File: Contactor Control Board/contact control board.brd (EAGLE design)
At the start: 75.9 x 50.8 mm, 36 parts, among them Q1 2n2222, Q2 2n2222, Q3 2n2222, Q4 MOSFET-NCHANNELFQP30N06L

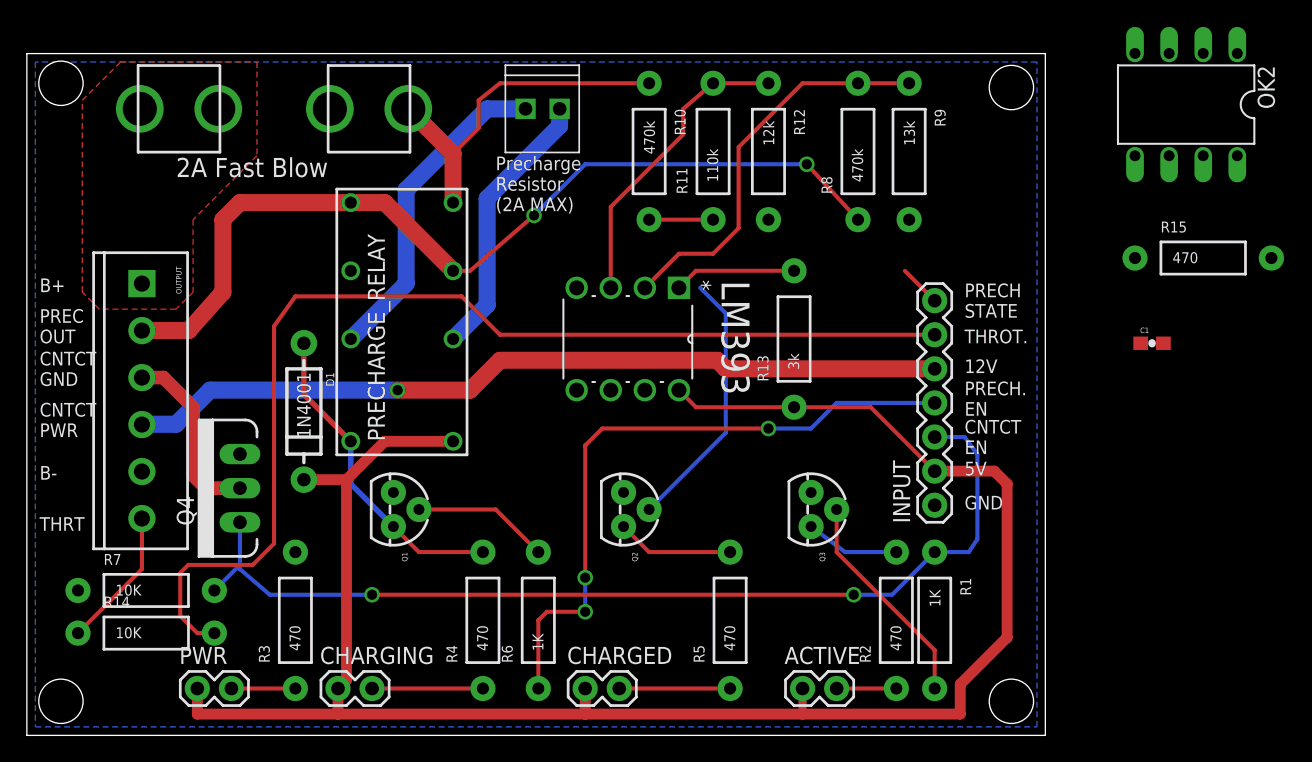
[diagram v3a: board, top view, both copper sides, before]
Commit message: Added buffer to use the output of the Op-Amp and split
it between an indicator LED and a digital signal output. Tested and
validated using breadboards
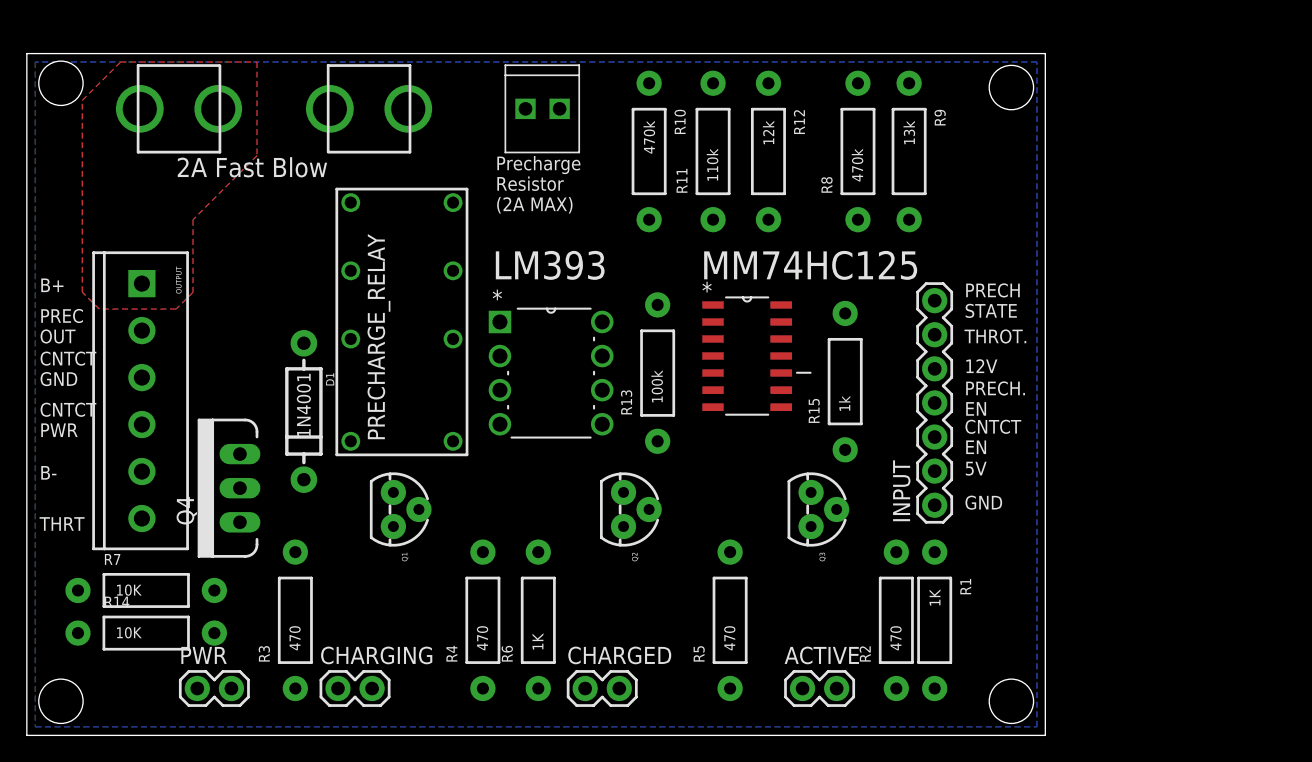
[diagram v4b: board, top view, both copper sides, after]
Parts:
- removed C1: 0.1uF, SparkFun-Capacitors:0603-CAP
- removed OK2: 6N138, optocoupler:DIL08
- added MM74HC125: MM74HC125M, Fairchild_By_element14_Batch_1:SOIC127P600X175-14N
- R13: value 3k -> 100k
- R15: value 470 -> 1k
- moved R15 28.2 mm to (61.0, 26.4), turned to 90 degrees
- moved R13 10.5 mm to (47.0, 27.0)
- moved LM393 3.17 mm to (42.9, 23.2), turned to 0 degrees
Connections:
- removed net PRECH_STATE: INPUT.7, OK2.6, Q2.2, R15.P$2
- removed net PRECH_STATE_TO_OPTO: LM393.1, OK2.2, R13.P$2
- new net N$6: MM74HC125.6, R15.P$2
- new net PRECH_STATE_LED: Q2.2, R15.P$1
- new net PRECH_STATE_OUT: INPUT.7, MM74HC125.3
- new net PRECH_STATE_TO_BUFF: LM393.1, MM74HC125.2, MM74HC125.5, R13.P$2
- net 5V: now also MM74HC125.14; no longer C1.1, OK2.8, R15.P$1
- net GND: now also MM74HC125.1, MM74HC125.4, MM74HC125.7; no longer C1.2, OK2.3, OK2.5
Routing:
- net 5V: track 138.5 -> 0.00 mm
- net THROTTLE: track 81.9 -> 0.00 mm
- net CONTACT_EN: track 73.8 -> 0.00 mm, vias 2 -> 0
- net PRECHARGE_OUT: track 67.6 -> 0.00 mm, vias 2 -> 0
- net 12V: track 61.3 -> 0.00 mm, vias 1 -> 0
- net PRECHARGE_EN: track 48.6 -> 0.00 mm, vias 3 -> 0
- net CAP_CHARGE_V_CURR: track 29.5 -> 0.00 mm
- net 72V_IN_FUSED: track 26.3 -> 0.00 mm
- net PRECHARGE_RESISTOR_OUT: track 24.2 -> 0.00 mm
- net PRECH_TRAN_COLLECTOR: track 23.9 -> 0.00 mm
- net PRECH_STATE: track 22.8 -> 0.00 mm
- net CAP_CHARGE_REF: track 22.6 -> 0.00 mm
- net PRECHARGE_RESISTOR_IN: track 20.4 -> 0.00 mm
- net N$2: track 16.4 -> 0.00 mm
- net CONTACT_GND: track 13.7 -> 0.00 mm
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
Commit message: Using the proper chip package for the buffer chip
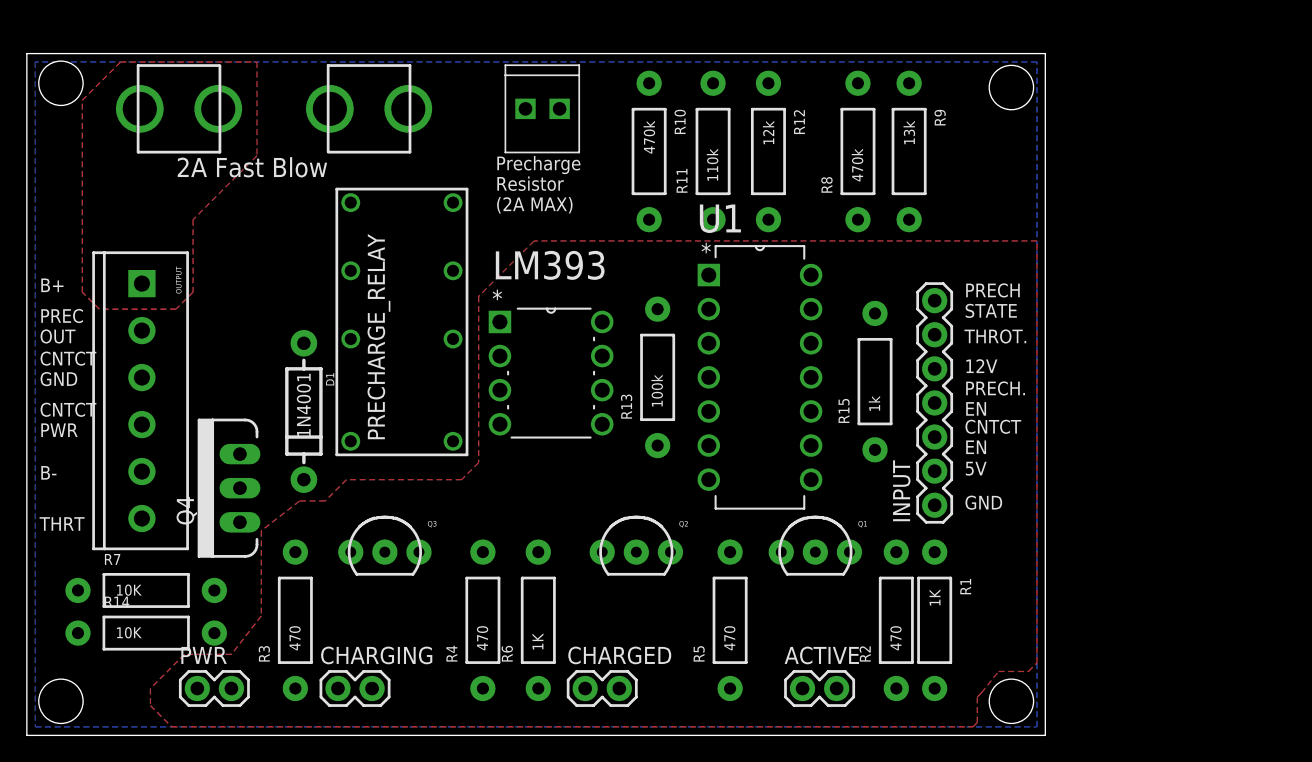
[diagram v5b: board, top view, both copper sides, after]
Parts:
- removed MM74HC125: MM74HC125M, Fairchild_By_element14_Batch_1:SOIC127P600X175-14N
- added U1: MM74HC125N, mm74hc125n:DIP254P762X533-14
- Q1, Q2, Q3: device SparkFun-DiscreteSemi:TO-92 -> SparkFun-DiscreteSemi:TO-92-AMMO
- moved Q3 31.9 mm to (26.7, 13.7), turned to 0 degrees
- moved Q1 31.6 mm to (58.7, 13.7), turned to 0 degrees
- moved Q2 3.31 mm to (45.4, 13.7), turned to 0 degrees
- moved R15 2.22 mm to (63.2, 26.4)
- moved R13 0.32 mm to (47.0, 26.7)
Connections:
- net 5V: now also U1.14; no longer MM74HC125.14
- net GND: now also U1.1, U1.4, U1.7; no longer MM74HC125.1, MM74HC125.4, MM74HC125.7
- net N$1: now also Q1.3; no longer Q3.3
- net N$2: now also Q1.2; no longer Q3.2
- net N$5: now also Q3.3; no longer Q2.3
- net N$6: now also U1.6; no longer MM74HC125.6
- net PRECH_STATE_LED: now also Q3.2; no longer Q2.2
- net PRECH_STATE_OUT: now also U1.3; no longer MM74HC125.3
- net PRECH_STATE_TO_BUFF: now also U1.2, U1.5; no longer MM74HC125.2, MM74HC125.5
- net PRECH_TRAN_COLLECTOR: now also Q2.3; no longer Q1.3
- net PRECH_TRAN_IN: now also Q2.2; no longer Q1.2
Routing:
- added copper zone on layer 1, net 5V

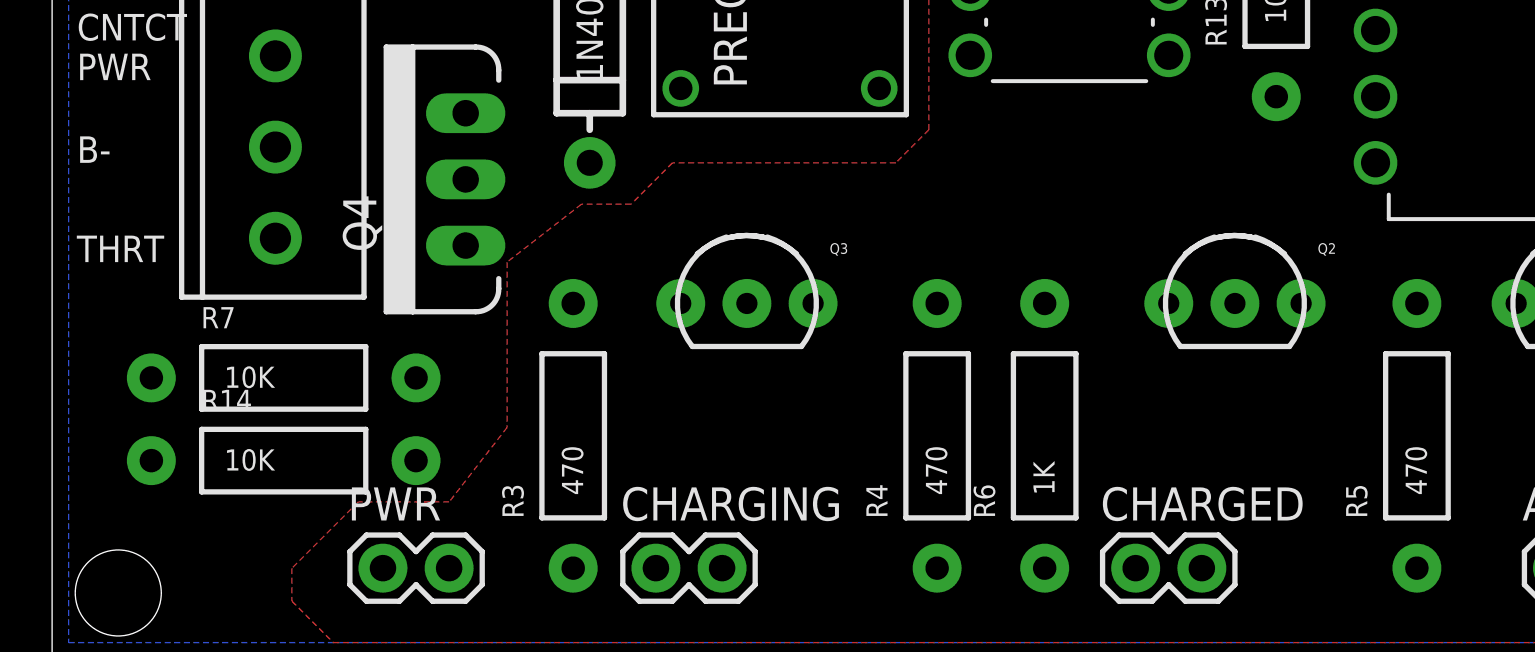
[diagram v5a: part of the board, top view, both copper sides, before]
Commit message: Updated precharge design
Replaced transistor with a FET as the Arduino can't source enough
current to trigger both the relay and the LED... At least not with the
transistors which were specced.
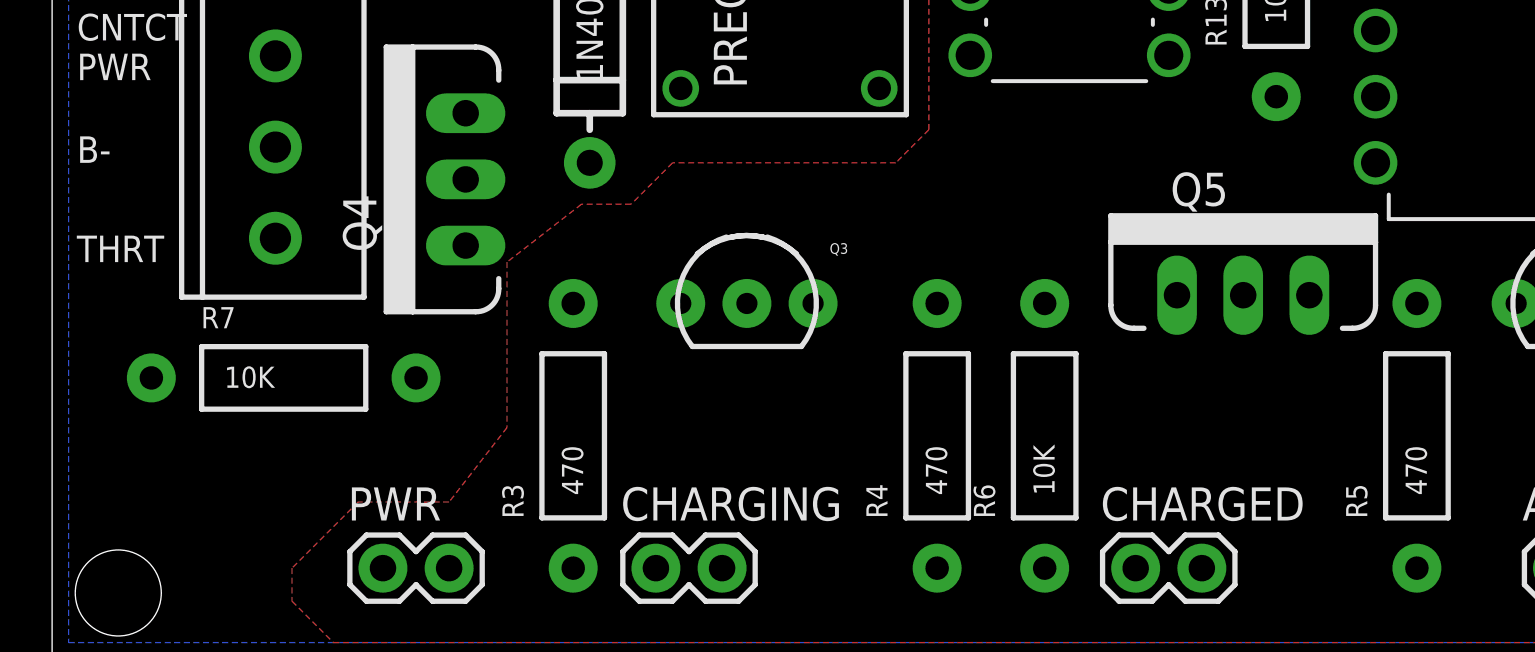
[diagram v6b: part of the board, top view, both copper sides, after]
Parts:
- removed Q2: 2n2222, SparkFun-DiscreteSemi:TO-92-AMMO
- removed R14: 10K, SparkFun-Resistors:AXIAL-0.4
- added Q5: MOSFET-NCHANNELFQP30N06L, SparkFun-DiscreteSemi:TO220V
- R6: value 1K -> 10K
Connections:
- removed net PRECH_TRAN_COLLECTOR: D1.A, PRECHARGE_RELAY.16, Q2.3, R4.P$2
- removed net PRECH_TRAN_IN: Q2.2, R6.P$2
- removed net THROTTLE_CURRENT_LIMITED: OUTPUT.6, R14.P$1
- new net PRECH_DRAIN: D1.A, PRECHARGE_RELAY.16, Q5.2, R4.P$2
- net GND: now also Q5.3, R6.P$1; no longer Q2.1
- net PRECHARGE_EN: now also Q5.1, R6.P$2; no longer R6.P$1
- net THROTTLE: now also OUTPUT.6; no longer R14.P$2
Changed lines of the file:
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@@
 <layer number="23" name="tOrigins" color="15" fill="1" visible="yes" active="yes"/>
 <layer number="24" name="bOrigins" color="15" fill="1" visible="yes" active="yes"/>
-<layer number="25" name="tNames" color="16" fill="1" visible="no" active="yes"/>
+<layer number="25" name="tNames" color="16" fill="1" visible="yes" active="yes"/>
 <layer number="26" name="bNames" color="16" fill="1" visible="no" active="yes"/>
 <layer number="27" name="tValues" color="7" fill="1" visible="no" active="yes"/>
@@
 <element name="R3" library="SparkFun-Resistors" package="AXIAL-0.4" value="470" x="20.0025" y="8.5725" rot="R90"/>
 <element name="R4" library="SparkFun-Resistors" package="AXIAL-0.4" value="470" x="33.9725" y="8.5725" rot="R90"/>
-<element name="R6" library="SparkFun-Resistors" package="AXIAL-0.4" value="1K" x="38.1" y="8.5725" rot="R90"/>
 <element name="R7" library="SparkFun-Resistors" package="AXIAL-0.4" value="10K" x="8.89" y="10.795"/>
 <element name="Q4" library="SparkFun-DiscreteSemi" package="TO220V" value="MOSFET-NCHANNELFQP30N06L" x="15.875" y="18.415" rot="R90">
@@
 <element name="CHARGED" library="SparkFun-Connectors" package="1X02" value="M02PTH" x="41.5925" y="3.4925"/>
 <element name="R5" library="SparkFun-Resistors" package="AXIAL-0.4" value="470" x="52.3875" y="8.5725" rot="R90"/>
-<element name="R14" library="SparkFun-Resistors" package="AXIAL-0.4" value="10K" x="8.89" y="7.62"/>
 <element name="R15" library="SparkFun-Resistors" package="AXIAL-0.4" value="1k" x="63.1825" y="26.3525" rot="R90"/>
 <element name="U1" library="mm74hc125n" package="DIP254P762X533-14" value="MM74HC125N" x="58.42" y="19.05">
@@
 <element name="Q3" library="SparkFun-DiscreteSemi" package="TO-92-AMMO" value="2n2222" x="26.67" y="13.6525"/>
 <element name="Q1" library="SparkFun-DiscreteSemi" package="TO-92-AMMO" value="2n2222" x="58.7375" y="13.6525"/>
-<element name="Q2" library="SparkFun-DiscreteSemi" package="TO-92-AMMO" value="2n2222" x="45.4025" y="13.6525"/>
+<element name="Q5" library="SparkFun-DiscreteSemi" package="TO220V" value="MOSFET-NCHANNELFQP30N06L" x="45.72" y="13.97">
+<attribute name="PROD_ID" value="TRANS-10060" x="45.72" y="13.97" size="1.778" layer="27" font="vector" ratio="15" display="off"/>
+</element>
+<element name="R6" library="SparkFun-Resistors" package="AXIAL-0.4" value="10K" x="38.1" y="8.5725" rot="R90"/>
 </elements>
 <signals>
@@
 <contactref element="ACTIVE" pad="1"/>
 <contactref element="PWR" pad="1"/>
-<contactref element="CHARGING" pad="1"/>
 <contactref element="D1" pad="C"/>
 <contactref element="R13" pad="P$1"/>
@@
 <vertex x="75.2475" y="5.3975"/>
 </polygon>
-<wire x1="42.8625" y1="30.7975" x2="58.42" y2="34.29" width="0" layer="19" extent="1-1"/>
-<wire x1="46.99" y1="21.59" x2="42.8625" y2="30.7975" width="0" layer="19" extent="1-1"/>
-<wire x1="31.75" y1="21.9075" x2="42.8625" y2="30.7975" width="0" layer="19" extent="1-1"/>
+<contactref element="CHARGING" pad="1"/>
 <wire x1="20.6375" y1="19.05" x2="31.75" y2="21.9075" width="0" layer="19" extent="1-1"/>
-<wire x1="23.1775" y1="3.4925" x2="20.6375" y2="19.05" width="0" layer="19" extent="1-1"/>
-<wire x1="12.7" y1="3.4925" x2="23.1775" y2="3.4925" width="0" layer="19" extent="1-1"/>
-<wire x1="67.6275" y1="19.685" x2="58.42" y2="34.29" width="0" layer="19" extent="1-1"/>
-<wire x1="41.5925" y1="3.4925" x2="23.1775" y2="3.4925" width="0" layer="19" extent="1-1"/>
-<wire x1="57.785" y1="3.4925" x2="41.5925" y2="3.4925" width="0" layer="19" extent="1-1"/>
+<wire x1="42.8625" y1="30.7975" x2="31.75" y2="21.9075" width="0" layer="19" extent="1-1"/>
 </signal>
 <signal name="GND">
@@
 <contactref element="Q3" pad="1"/>
 <contactref element="Q1" pad="1"/>
-<contactref element="Q2" pad="1"/>
-<wire x1="55.245" y1="38.4175" x2="65.7225" y2="38.4175" width="0" layer="19" extent="1-1"/>
-<wire x1="50.8" y1="34.29" x2="55.245" y2="38.4175" width="0" layer="19" extent="1-1"/>
-<wire x1="50.8" y1="26.67" x2="50.8" y2="34.29" width="0" layer="19" extent="1-1"/>
-<wire x1="50.8" y1="19.05" x2="50.8" y2="26.67" width="0" layer="19" extent="1-1"/>
-<wire x1="56.1975" y1="13.6525" x2="50.8" y2="19.05" width="0" layer="19" extent="1-1"/>
-<wire x1="42.8625" y1="13.6525" x2="50.8" y2="19.05" width="0" layer="19" extent="1-1"/>
-<wire x1="67.6275" y1="17.145" x2="56.1975" y2="13.6525" width="0" layer="19" extent="1-1"/>
-<wire x1="35.2425" y1="23.1775" x2="42.8625" y2="13.6525" width="0" layer="19" extent="1-1"/>
-<wire x1="24.13" y1="13.6525" x2="35.2425" y2="23.1775" width="0" layer="19" extent="1-1"/>
-<wire x1="20.0025" y1="13.6525" x2="24.13" y2="13.6525" width="0" layer="19" extent="1-1"/>
-<wire x1="15.875" y1="20.955" x2="20.0025" y2="13.6525" width="0" layer="19" extent="1-1"/>
-<wire x1="8.5725" y1="19.655" x2="15.875" y2="20.955" width="0" layer="19" extent="1-1"/>
-<wire x1="3.81" y1="10.795" x2="8.5725" y2="19.655" width="0" layer="19" extent="1-1"/>
-<wire x1="24.13" y1="34.6075" x2="35.2425" y2="23.1775" width="0" layer="19" extent="1-1"/>
+<contactref element="Q5" pad="3"/>
+<contactref element="R6" pad="P$1"/>
 </signal>
 <signal name="CONTACT_EN">
@@
 </signal>
 <signal name="PRECHARGE_EN">
-<contactref element="R6" pad="P$1"/>
 <contactref element="INPUT" pad="4"/>
-<wire x1="38.1" y1="3.4925" x2="67.6275" y2="24.765" width="0" layer="19" extent="1-1"/>
+<contactref element="Q5" pad="1"/>
+<contactref element="R6" pad="P$2"/>
+<wire x1="43.18" y1="13.97" x2="67.6275" y2="24.765" width="0" layer="19" extent="1-1"/>
+<wire x1="38.1" y1="13.6525" x2="43.18" y2="13.97" width="0" layer="19" extent="1-1"/>
 </signal>
 <signal name="12V">
@@
 <signal name="THROTTLE">
 <contactref element="INPUT" pad="6"/>
-<contactref element="R14" pad="P$2"/>
-<wire x1="13.97" y1="7.62" x2="67.6275" y2="29.845" width="0" layer="19" extent="1-1"/>
+<contactref element="OUTPUT" pad="6"/>
+<wire x1="8.5725" y1="16.155" x2="67.6275" y2="29.845" width="0" layer="19" extent="1-1"/>
 </signal>
 <signal name="72V_IN">
@@
 <vertex x="6.985" y="50.165"/>
 </polygon>
-<wire x1="8.5725" y1="33.655" x2="14.257" y2="46.6725" width="0" layer="19" extent="1-1"/>
 </signal>
 <signal name="PRECHARGE_OUT">
@@
 <wire x1="15.24" y1="3.4925" x2="20.0025" y2="3.4925" width="0" layer="19" extent="1-1"/>
 </signal>
-<signal name="N$14">
-<contactref element="R4" pad="P$1"/>
-<contactref element="CHARGING" pad="2"/>
-<wire x1="25.7175" y1="3.4925" x2="33.9725" y2="3.4925" width="0" layer="19" extent="1-1"/>
-</signal>
 <signal name="72V_IN_FUSED">
 <contactref element="PRECHARGE_FUSE" pad="1"/>
@@
 <wire x1="61.2775" y1="13.6525" x2="64.77" y2="13.6525" width="0" layer="19" extent="1-1"/>
 </signal>
-<signal name="PRECH_TRAN_COLLECTOR">
-<contactref element="R4" pad="P$2"/>
+<signal name="PRECH_DRAIN">
 <contactref element="D1" pad="A"/>
 <contactref element="PRECHARGE_RELAY" pad="16"/>
-<contactref element="Q2" pad="3"/>
-<wire x1="33.9725" y1="13.6525" x2="47.9425" y2="13.6525" width="0" layer="19" extent="1-1"/>
+<contactref element="R4" pad="P$2"/>
+<contactref element="Q5" pad="2"/>
+<wire x1="33.9725" y1="13.6525" x2="45.72" y2="13.97" width="0" layer="19" extent="1-1"/>
 <wire x1="24.13" y1="21.9075" x2="33.9725" y2="13.6525" width="0" layer="19" extent="1-1"/>
 <wire x1="20.6375" y1="29.21" x2="24.13" y2="21.9075" width="0" layer="19" extent="1-1"/>
@@
 <wire x1="67.6275" y1="3.4925" x2="58.7375" y2="13.6525" width="0" layer="19" extent="1-1"/>
 </signal>
-<signal name="PRECH_TRAN_IN">
-<contactref element="R6" pad="P$2"/>
-<contactref element="Q2" pad="2"/>
-<wire x1="38.1" y1="13.6525" x2="45.4025" y2="13.6525" width="0" layer="19" extent="1-1"/>
-</signal>
 <signal name="N$4">
 <contactref element="CHARGED" pad="2"/>
@@
 <contactref element="Q3" pad="3"/>
 <wire x1="29.21" y1="13.6525" x2="52.3875" y2="13.6525" width="0" layer="19" extent="1-1"/>
-</signal>
-<signal name="THROTTLE_CURRENT_LIMITED">
-<contactref element="OUTPUT" pad="6"/>
-<contactref element="R14" pad="P$1"/>
-<wire x1="3.81" y1="7.62" x2="8.5725" y2="16.155" width="0" layer="19" extent="1-1"/>
 </signal>
 <signal name="PRECH_STATE_TO_BUFF">
@@
 <wire x1="50.8" y1="21.59" x2="63.1825" y2="31.4325" width="0" layer="19" extent="1-1"/>
 </signal>
+<signal name="N$7">
+<contactref element="CHARGING" pad="2"/>
+<contactref element="R4" pad="P$1"/>
+<wire x1="25.7175" y1="3.4925" x2="33.9725" y2="3.4925" width="0" layer="19" extent="1-1"/>
+</signal>
 </signals>
